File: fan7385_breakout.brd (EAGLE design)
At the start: 28.6 x 15.2 mm, 17 parts

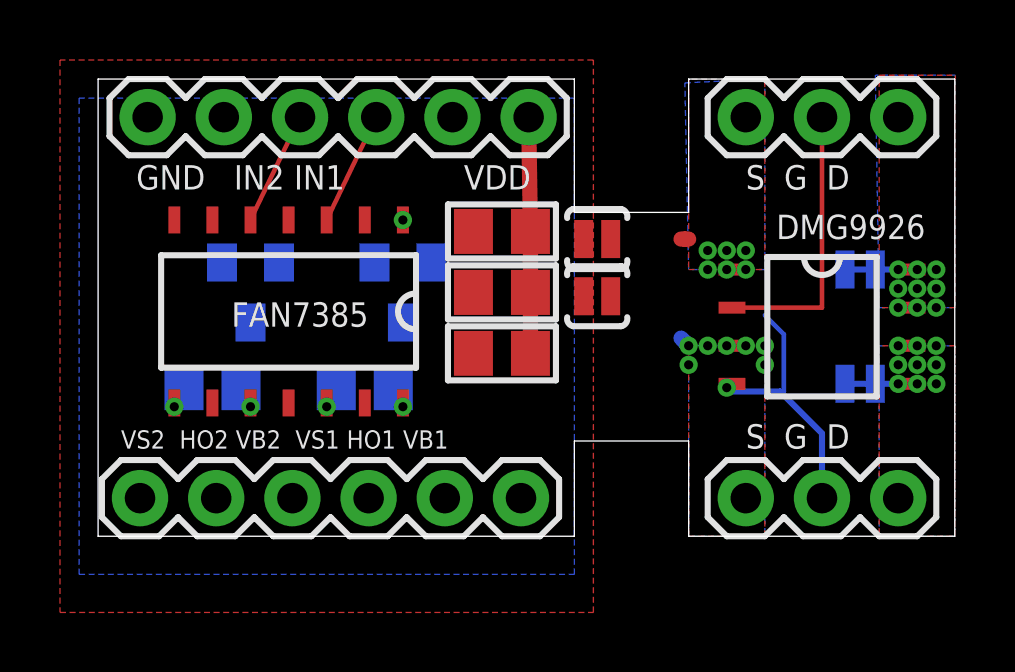
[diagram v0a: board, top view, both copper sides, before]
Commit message: removed a cap to help with routing
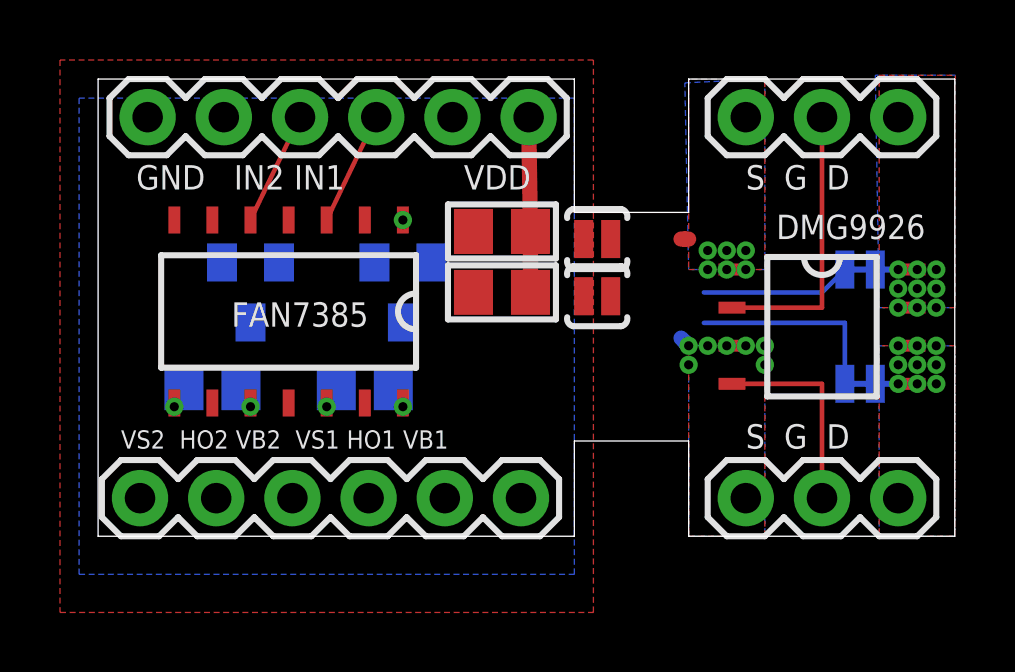
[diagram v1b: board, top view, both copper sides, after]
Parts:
- removed CVDD2: 0.1uF 25V, microbuilder:0805
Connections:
- net GND: no longer CVDD2.1
- net VDD: no longer CVDD2.2
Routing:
- net VS2: track 0.00 -> 6.73 mm
- net VS1: track 0.00 -> 5.01 mm
- net HO2/G2: track 9.27 -> 6.81 mm, vias 1 -> 0
- net VDD: track 7.87 -> 5.84 mm
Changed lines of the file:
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@@
 <setting verticaltext="up"/>
 </settings>
-<grid distance="50" unitdist="mil" unit="mil" style="lines" multiple="1" display="yes" altdistance="0.025" altunitdist="inch" altunit="inch"/>
+<grid distance="5" unitdist="mil" unit="mil" style="lines" multiple="1" display="yes" altdistance="0.025" altunitdist="inch" altunit="inch"/>
 <layers>
 <layer number="1" name="Top" color="4" fill="1" visible="yes" active="yes"/>
@@
 </element>
 <element name="CVDD1" library="microbuilder" package="0805" value="0.1uF 25V" x="13.462" y="8.128" smashed="yes"/>
-<element name="CVDD2" library="microbuilder" package="0805" value="0.1uF 25V" x="13.462" y="6.096" smashed="yes"/>
 </elements>
 <signals>
@@
 <contactref element="JP1" pad="1"/>
 <contactref element="CVDD1" pad="1"/>
-<contactref element="CVDD2" pad="1"/>
 </signal>
 <signal name="VDD" class="2">
@@
 <contactref element="JP1" pad="5"/>
 <contactref element="CVDD1" pad="2"/>
-<contactref element="CVDD2" pad="2"/>
 <via x="10.16" y="10.541" extent="1-16" drill="0.3048" shape="square"/>
 <wire x1="14.351" y1="13.97" x2="14.412" y2="10.16" width="0.508" layer="1"/>
 <wire x1="14.412" y1="10.16" x2="14.412" y2="8.128" width="0.508" layer="1"/>
-<wire x1="14.412" y1="8.128" x2="14.412" y2="6.096" width="0.508" layer="1"/>
 <wire x1="14.412" y1="10.16" x2="16.187" y2="9.906" width="0" layer="19" extent="1-1"/>
 <wire x1="16.187" y1="8.001" x2="14.412" y2="8.128" width="0" layer="19" extent="1-1"/>
@@
 <contactref element="GATEDRV" pad="9"/>
 <contactref element="FET" pad="4"/>
-<via x="20.955" y="4.953" extent="1-16" drill="0.3048" shape="square"/>
-<wire x1="24.13" y1="3.429" x2="22.7965" y2="4.7625" width="0.2032" layer="16"/>
-<wire x1="22.7965" y1="4.7625" x2="22.733" y2="4.826" width="0.2032" layer="16"/>
-<wire x1="22.733" y1="4.826" x2="21.082" y2="4.826" width="0.2032" layer="16"/>
-<wire x1="21.082" y1="4.826" x2="20.955" y2="4.953" width="0.2032" layer="16"/>
-<wire x1="21.13" y1="5.08" x2="21.082" y2="5.08" width="0.2032" layer="1"/>
-<wire x1="21.082" y1="5.08" x2="20.955" y2="4.953" width="0.2032" layer="1"/>
 <contactref element="JP2" pad="2"/>
 <contactref element="JP3" pad="2"/>
-<wire x1="24.13" y1="3.429" x2="24.13" y2="1.27" width="0.2032" layer="16"/>
-<wire x1="20.955" y1="4.953" x2="20.828" y2="5.08" width="0.1524" layer="16"/>
-<wire x1="22.86" y1="6.731" x2="22.225" y2="7.366" width="0.1524" layer="16"/>
-<wire x1="22.86" y1="4.826" x2="22.86" y2="6.731" width="0.1524" layer="16"/>
-<wire x1="22.86" y1="4.826" x2="22.7965" y2="4.7625" width="0.1524" layer="16"/>
-<wire x1="3.81" y1="4.443" x2="20.828" y2="5.08" width="0" layer="19" extent="1-16"/>
+<wire x1="21.13" y1="5.08" x2="24.13" y2="5.08" width="0.1524" layer="1"/>
+<wire x1="24.13" y1="5.08" x2="24.13" y2="1.27" width="0.1524" layer="1"/>
+<wire x1="3.81" y1="4.443" x2="21.13" y2="5.08" width="0" layer="19" extent="1-1"/>
 <wire x1="3.937" y1="1.27" x2="3.81" y2="4.443" width="0" layer="19" extent="1-1"/>
 </signal>
@@
 <contactref element="JP2" pad="4"/>
 <via x="7.62" y="4.318" extent="1-16" drill="0.3048" shape="square"/>
-<wire x1="7.94" y1="4.953" x2="24.892" y2="8.89" width="0" layer="19" extent="16-16"/>
+<wire x1="24.892" y1="8.89" x2="24.13" y2="8.128" width="0.1524" layer="16"/>
+<wire x1="24.13" y1="8.128" x2="20.193" y2="8.128" width="0.1524" layer="16"/>
+<wire x1="7.94" y1="4.953" x2="20.193" y2="8.128" width="0" layer="19" extent="16-16"/>
 <wire x1="7.62" y1="4.443" x2="7.94" y2="4.953" width="0" layer="19" extent="1-16"/>
 <wire x1="7.62" y1="4.318" x2="7.62" y2="4.443" width="0" layer="19" extent="1-1"/>
@@
 <contactref element="JP2" pad="1"/>
 <via x="2.54" y="4.318" extent="1-16" drill="0.3048" shape="square"/>
-<wire x1="2.86" y1="4.953" x2="24.892" y2="5.08" width="0" layer="19" extent="16-16"/>
+<wire x1="24.892" y1="5.08" x2="24.892" y2="7.112" width="0.1524" layer="16"/>
+<wire x1="24.892" y1="7.112" x2="20.193" y2="7.112" width="0.1524" layer="16"/>
+<wire x1="2.86" y1="4.953" x2="20.193" y2="7.112" width="0" layer="19" extent="16-16"/>
 <wire x1="2.54" y1="4.443" x2="2.86" y2="4.953" width="0" layer="19" extent="1-16"/>
 <wire x1="2.54" y1="4.318" x2="2.54" y2="4.443" width="0" layer="19" extent="1-1"/>

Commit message: two cap routing
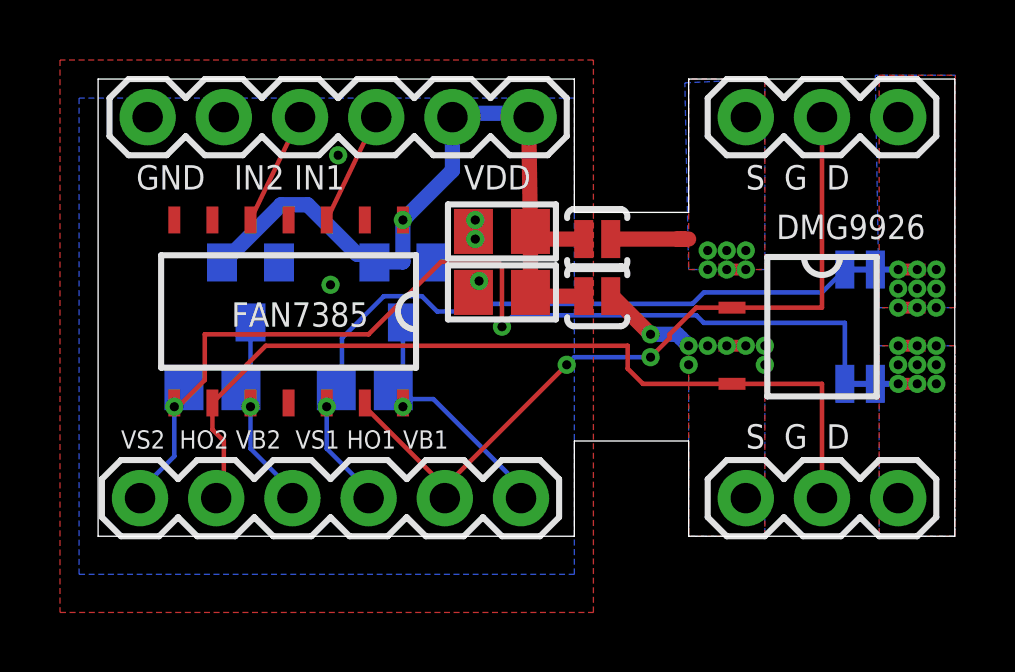
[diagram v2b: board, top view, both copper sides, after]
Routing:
- net VS2: track 6.73 -> 34.3 mm, vias 1 -> 2
- net HO2/G2: track 6.81 -> 29.4 mm
- net VDD: track 5.84 -> 25.6 mm
- net VS1: track 5.01 -> 24.7 mm
- net HO1/G1: track 9.35 -> 26.1 mm, vias 0 -> 2
- net VB1: track 0.00 -> 9.36 mm
- net VB2: track 0.00 -> 7.20 mm
- net S2: track 0.54 -> 3.46 mm, vias 7 -> 8
- net S1: track 0.25 -> 2.60 mm

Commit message: routed
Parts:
- added CVDD2: 0.1uF 25V, microbuilder:0805
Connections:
- net GND: now also CVDD2.1
- net VDD: now also CVDD2.2
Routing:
- net VDD: track 25.6 -> 29.1 mm, vias 1 -> 4
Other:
- outline, holes or cut-outs redrawn
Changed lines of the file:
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@@
 <setting verticaltext="up"/>
 </settings>
-<grid distance="5" unitdist="mil" unit="mil" style="lines" multiple="1" display="yes" altdistance="0.025" altunitdist="inch" altunit="inch"/>
+<grid distance="2.5" unitdist="mil" unit="mil" style="lines" multiple="1" display="yes" altdistance="0.025" altunitdist="inch" altunit="inch"/>
 <layers>
 <layer number="1" name="Top" color="4" fill="1" visible="yes" active="yes"/>
@@
 <plain>
 <wire x1="0" y1="0" x2="15.875" y2="0" width="0" layer="20"/>
-<wire x1="15.875" y1="0" x2="15.875" y2="3.175" width="0" layer="20"/>
-<wire x1="15.875" y1="3.175" x2="19.685" y2="3.175" width="0" layer="20"/>
-<wire x1="19.685" y1="3.175" x2="19.685" y2="0" width="0" layer="20"/>
+<wire x1="15.875" y1="0" x2="15.875" y2="4.445" width="0" layer="20"/>
+<wire x1="15.875" y1="4.445" x2="19.685" y2="4.445" width="0" layer="20"/>
+<wire x1="19.685" y1="4.445" x2="19.685" y2="0" width="0" layer="20"/>
 <wire x1="19.685" y1="0" x2="28.555" y2="0" width="0" layer="20"/>
 <wire x1="28.555" y1="0" x2="28.555" y2="15.24" width="0" layer="20"/>
@@
 </element>
 <element name="CVDD1" library="microbuilder" package="0805" value="0.1uF 25V" x="13.462" y="8.128" smashed="yes"/>
+<element name="CVDD2" library="microbuilder" package="0805" value="0.1uF 25V" x="13.462" y="5.08" smashed="yes"/>
 </elements>
 <signals>
@@
 <via x="8.001" y="12.7" extent="1-16" drill="0.3048" shape="octagon"/>
 <via x="7.747" y="8.382" extent="1-16" drill="0.3048" shape="octagon"/>
+<contactref element="CVDD2" pad="1"/>
+<via x="12.573" y="5.588" extent="1-16" drill="0.3048" shape="square"/>
+<via x="12.573" y="4.953" extent="1-16" drill="0.3048" shape="square"/>
+<via x="12.573" y="6.985" extent="1-16" drill="0.3048" shape="square"/>
 </signal>
 <signal name="VDD" class="2">
@@
 <wire x1="4.191" y1="9.144" x2="4.13" y2="9.128" width="0.508" layer="16"/>
 <wire x1="9.271" y1="9.398" x2="9.21" y2="9.128" width="0.508" layer="16"/>
-<wire x1="14.605" y1="8.001" x2="16.129" y2="8.001" width="0.508" layer="1"/>
-<wire x1="16.129" y1="8.001" x2="16.187" y2="8.001" width="0.508" layer="1"/>
-<wire x1="14.605" y1="8.001" x2="14.412" y2="8.128" width="0.508" layer="1"/>
 <wire x1="14.605" y1="9.906" x2="16.129" y2="9.906" width="0.508" layer="1"/>
 <wire x1="16.129" y1="9.906" x2="16.187" y2="9.906" width="0.508" layer="1"/>
@@
 <wire x1="10.287" y1="10.668" x2="10.16" y2="10.541" width="0.508" layer="16"/>
 <wire x1="11.811" y1="13.843" x2="11.811" y2="13.97" width="0.508" layer="16"/>
+<contactref element="CVDD2" pad="2"/>
+<wire x1="14.412" y1="8.128" x2="16.187" y2="8.128" width="0.508" layer="1"/>
+<wire x1="16.187" y1="8.128" x2="16.187" y2="8.001" width="0.508" layer="1"/>
+<wire x1="14.412" y1="8.128" x2="14.478" y2="8.128" width="0.508" layer="1"/>
+<wire x1="14.478" y1="8.128" x2="14.478" y2="6.7945" width="0.508" layer="1"/>
+<via x="14.478" y="6.7945" extent="1-16" drill="0.3048"/>
+<wire x1="14.478" y1="6.7945" x2="14.478" y2="5.715" width="0.508" layer="16"/>
+<via x="14.478" y="5.461" extent="1-16" drill="0.3048" shape="square"/>
+<via x="14.478" y="4.826" extent="1-16" drill="0.3048" shape="square"/>
+<wire x1="14.478" y1="5.461" x2="14.412" y2="5.461" width="0.508" layer="1"/>
+<wire x1="14.412" y1="5.461" x2="14.412" y2="5.08" width="0.508" layer="1"/>
+<wire x1="14.478" y1="4.826" x2="14.412" y2="4.826" width="0.508" layer="1"/>
+<wire x1="14.412" y1="4.826" x2="14.412" y2="5.08" width="0.508" layer="1"/>
+<wire x1="14.478" y1="5.715" x2="14.478" y2="5.461" width="0.508" layer="16"/>
 </signal>
 <signal name="S1" class="2">
@@
 <wire x1="11.557" y1="1.27" x2="11.557" y2="1.651" width="0.1524" layer="1"/>
 <wire x1="8.89" y1="4.318" x2="8.89" y2="4.443" width="0.1524" layer="1"/>
-<wire x1="15.621" y1="5.715" x2="11.557" y2="1.651" width="0.1524" layer="1"/>
-<wire x1="15.875" y1="5.969" x2="15.621" y2="5.715" width="0.1524" layer="16"/>
+<wire x1="13.335" y1="3.429" x2="11.557" y2="1.651" width="0.1524" layer="1"/>
+<wire x1="15.875" y1="5.969" x2="15.494" y2="4.826" width="0.1524" layer="16"/>
+<wire x1="15.494" y1="4.826" x2="14.097" y2="3.429" width="0.1524" layer="16"/>
+<wire x1="14.097" y1="3.429" x2="13.335" y2="3.429" width="0.1524" layer="16"/>
 <wire x1="18.415" y1="5.969" x2="15.875" y2="5.969" width="0.1524" layer="16"/>
 <wire x1="19.05" y1="6.604" x2="18.415" y2="5.969" width="0.1524" layer="1"/>
@@
 <wire x1="11.557" y1="1.651" x2="11.557" y2="1.27" width="0.1524" layer="1"/>
 <wire x1="21.082" y1="7.62" x2="21.13" y2="7.62" width="0.1524" layer="1"/>
-<via x="15.621" y="5.715" extent="1-16" drill="0.3048"/>
+<via x="13.335" y="3.429" extent="1-16" drill="0.3048"/>
 <via x="18.415" y="5.969" extent="1-16" drill="0.3048"/>
 </signal>
@@
 <wire x1="4.953" y1="5.588" x2="3.81" y2="4.445" width="0.1524" layer="1"/>
 <wire x1="4.953" y1="5.715" x2="4.953" y2="5.588" width="0.1524" layer="1"/>
-<wire x1="5.588" y1="6.35" x2="4.953" y2="5.715" width="0.1524" layer="1"/>
-<wire x1="17.653" y1="6.35" x2="5.588" y2="6.35" width="0.1524" layer="1"/>
-<wire x1="17.653" y1="5.588" x2="17.653" y2="6.35" width="0.1524" layer="1"/>
+<wire x1="5.588" y1="6.223" x2="4.953" y2="5.715" width="0.1524" layer="1"/>
+<wire x1="17.653" y1="6.223" x2="5.588" y2="6.223" width="0.1524" layer="1"/>
+<wire x1="17.653" y1="5.588" x2="17.653" y2="6.223" width="0.1524" layer="1"/>
 <wire x1="18.161" y1="5.08" x2="17.653" y2="5.588" width="0.1524" layer="1"/>
 <wire x1="21.082" y1="5.08" x2="18.161" y2="5.08" width="0.1524" layer="1"/>
@@
 </signal>
 </signals>
+<errors>
+</errors>
 </board>
 </drawing>

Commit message: one more change
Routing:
- net S2: vias 8 -> 14
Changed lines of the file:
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@@
 <setting verticaltext="up"/>
 </settings>
-<grid distance="2.5" unitdist="mil" unit="mil" style="lines" multiple="1" display="yes" altdistance="0.025" altunitdist="inch" altunit="inch"/>
+<grid distance="5" unitdist="mil" unit="mil" style="lines" multiple="1" display="yes" altdistance="0.025" altunitdist="inch" altunit="inch"/>
 <layers>
 <layer number="1" name="Top" color="4" fill="1" visible="yes" active="yes"/>
@@
 <wire x1="19.304" y1="6.731" x2="19.431" y2="6.604" width="0.508" layer="16"/>
 <via x="18.415" y="6.731" extent="1-16" drill="0.3048"/>
+<via x="22.225" y="4.445" extent="1-16" drill="0.3048" shape="square"/>
+<via x="20.066" y="4.445" extent="1-16" drill="0.3048" shape="square"/>
+<via x="20.32" y="3.81" extent="1-16" drill="0.3048" shape="square"/>
+<via x="20.955" y="3.81" extent="1-16" drill="0.3048" shape="square"/>
+<via x="21.59" y="3.81" extent="1-16" drill="0.3048" shape="square"/>
+<via x="22.225" y="3.81" extent="1-16" drill="0.3048" shape="square"/>
 </signal>
 <signal name="IN1">
